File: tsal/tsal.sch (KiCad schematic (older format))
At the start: 9 parts, among them Q1 TIP120, Q2 TIP120

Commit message: TSAL Done in a sane manner - schematic, footprint associations and BOM good. No PCB yet
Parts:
- removed D1: 26V, symbol D_Zener
- removed D2: TSAL, symbol LED
- removed Q1, Q2: TIP120, TO-220, symbol TIP120
- removed R1, R4: 1R, symbol R
- removed R2: 100R, symbol R
- removed R3: 15k, symbol R
- added C1, C3: 10u, Capacitors_ThroughHole:CP_Radial_D5.0mm_P2.00mm, symbol C
- added C2, C4: 1u, Capacitors_ThroughHole:C_Rect_L7.2mm_W5.5mm_P5.00mm_FKS2_FKP2_MKS2_MKP2, symbol C
- added P1: TS+, Wire_Pads:SolderWirePad_single_2mmDrill, symbol CONN_01X01
- added P2: TS-, Wire_Pads:SolderWirePad_single_2mmDrill, symbol CONN_01X01
- added P3: +12V, Wire_Pads:SolderWirePad_2x_2mmDrill, symbol CONN_01X02
- added P4: TS-, Wire_Pads:SolderWirePad_2x_2mmDrill, symbol CONN_01X02
- added U1: V36SE12004NRFA, UNCAMotorsports:V36SE12004NRFA, symbol V36SE12004NRFA
- F1: value 3A -> Fuse; footprint (none) -> Fuse_Holders_and_Fuses:Fuse_SMD1206_HandSoldering
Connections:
- net labels added: GND
- net labels removed: TractiveSystem+, TractiveSystem-
- wire segments 12 -> 18
- no-connect marks 0 -> 1

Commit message: TSAL Updates
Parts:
- added P5: TS+ (PostAIR), Wire_Pads:SolderWirePad_single_1mmDrill, symbol CONN_01X01
- added R1: 10k, Resistors_SMD:R_0805_HandSoldering, symbol R
- added R2: 1k, Resistors_SMD:R_0805_HandSoldering, symbol R
- added U2: TL431, symbol TL431
- P1: value TS+ -> TS+ (PreAIR)
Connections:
- net GND: now also R2.2, U2.3 (A); no longer U1.2 (ON/OFF)
- new net: U1.2 (ON/OFF), U2.1 (C)
- new net: R1.2, R2.1, U2.2 (REF)
- new net: P5.1 (P1), R1.1
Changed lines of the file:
@@
 	1    0    0    -1
 $EndComp
-Wire Wire Line
-	3400 3400 3400 3850
-Wire Wire Line
-	1600 3700 3400 3700
-Wire Wire Line
-	2250 3100 3400 3100
-Connection ~ 3400 3400
-Connection ~ 3400 3700
 NoConn ~ 4600 3400
-Wire Wire Line
-	4600 3250 4600 3100
-Wire Wire Line
-	4600 3550 4600 3850
-Connection ~ 4600 3250
-Connection ~ 4600 3100
-Connection ~ 4600 3550
-Connection ~ 4600 3700
-Connection ~ 3400 3100
-Wire Wire Line
-	4600 3100 6350 3100
-Wire Wire Line
-	4600 3700 6350 3700
 $Comp
 L C C2
@@
 	1    0    0    -1
 $EndComp
-Wire Wire Line
-	5150 3100 5150 3250
-Wire Wire Line
-	5500 3100 5500 3250
-Connection ~ 5150 3100
-Wire Wire Line
-	5150 3700 5150 3550
-Wire Wire Line
-	5500 3700 5500 3550
-Connection ~ 5150 3700
-Wire Wire Line
-	2850 3100 2850 3250
-Wire Wire Line
-	2850 3700 2850 3550
-Wire Wire Line
-	2500 3100 2500 3250
-Connection ~ 2850 3100
-Wire Wire Line
-	2500 3550 2500 3700
-Connection ~ 2850 3700
 $Comp
 L Fuse F1
@@
 	0    1    1    0
 $EndComp
-Connection ~ 2500 3100
-Connection ~ 2500 3700
 $Comp
 L GND #PWR01
@@
 	1    0    0    -1
 $EndComp
-Wire Wire Line
-	6350 3200 5500 3200
-Connection ~ 5500 3200
-Connection ~ 5500 3100
-Wire Wire Line
-	6350 3600 5500 3600
-Connection ~ 5500 3600
-Connection ~ 5500 3700
 $Comp
 L CONN_01X01 P1
@@
 P 1400 3100
 F 0 "P1" H 1319 2875 50  0000 C CNN
-F 1 "TS+" H 1319 2966 50  0000 C CNN
+F 1 "TS+ (PreAIR)" H 1319 2966 50  0000 C CNN
 F 2 "Wire_Pads:SolderWirePad_single_2mmDrill" H 1400 3100 50  0001 C CNN
 F 3 "" H 1400 3100 50  0000 C CNN
@@
 	-1   0    0    1
 $EndComp
-Wire Wire Line
-	1600 3100 1950 3100
 $Comp
 L PWR_FLAG #FLG03
@@
 	1    0    0    -1
 $EndComp
-Connection ~ 1750 3100
+$Comp
+L TL431 U2
+U 1 1 58AFA4D2
+P 2550 4500
+F 0 "U2" H 2371 4553 60  0000 R CNN
+F 1 "TL431" H 2371 4447 60  0000 R CNN
+F 2 "" H 2550 4450 60  0001 C CNN
+F 3 "" H 2550 4450 60  0000 C CNN
+	1    2550 4500
+	-1   0    0    -1
+$EndComp
+$Comp
+L R R1
+U 1 1 58AFA803
+P 2050 4250
+F 0 "R1" H 2120 4296 50  0000 L CNN
+F 1 "10k" H 2120 4205 50  0000 L CNN
+F 2 "Resistors_SMD:R_0805_HandSoldering" V 1980 4250 50  0001 C CNN
+F 3 "" H 2050 4250 50  0000 C CNN
+	1    2050 4250
+	1    0    0    -1
+$EndComp
+$Comp
+L R R2
+U 1 1 58AFA870
+P 2050 4750
+F 0 "R2" H 2120 4796 50  0000 L CNN
+F 1 "1k" H 2120 4705 50  0000 L CNN
+F 2 "Resistors_SMD:R_0805_HandSoldering" V 1980 4750 50  0001 C CNN
+F 3 "" H 2050 4750 50  0000 C CNN
+	1    2050 4750
+	1    0    0    -1
+$EndComp
+$Comp
+L GND #PWR04
+U 1 1 58AFA9A0
+P 2050 5150
+F 0 "#PWR04" H 2050 4900 50  0001 C CNN
+F 1 "GND" H 2055 4977 50  0000 C CNN
+F 2 "" H 2050 5150 50  0000 C CNN
+F 3 "" H 2050 5150 50  0000 C CNN
+	1    2050 5150
+	1    0    0    -1
+$EndComp
+$Comp
+L GND #PWR05
+U 1 1 58AFA9D5
+P 2550 5150
+F 0 "#PWR05" H 2550 4900 50  0001 C CNN
+F 1 "GND" H 2555 4977 50  0000 C CNN
+F 2 "" H 2550 5150 50  0000 C CNN
+F 3 "" H 2550 5150 50  0000 C CNN
+	1    2550 5150
+	1    0    0    -1
+$EndComp
+Wire Wire Line
+	1600 3700 3400 3700
+Wire Wire Line
+	2250 3100 3400 3100
+Connection ~ 3400 3700
+Wire Wire Line
+	4600 3250 4600 3100
+Wire Wire Line
+	4600 3550 4600 3850
+Connection ~ 4600 3250
+Connection ~ 4600 3100
+Connection ~ 4600 3550
+Connection ~ 4600 3700
+Connection ~ 3400 3100
+Wire Wire Line
+	4600 3100 6350 3100
+Wire Wire Line
+	4600 3700 6350 3700
+Wire Wire Line
+	5150 3100 5150 3250
+Wire Wire Line
+	5500 3100 5500 3250
+Connection ~ 5150 3100
+Wire Wire Line
+	5150 3700 5150 3550
+Wire Wire Line
+	5500 3700 5500 3550
+Connection ~ 5150 3700
+Wire Wire Line
+	2850 3100 2850 3250
+Wire Wire Line
+	2850 3700 2850 3550
+Wire Wire Line
+	2500 3100 2500 3250
+Connection ~ 2850 3100
+Wire Wire Line
+	2500 3550 2500 3700
+Connection ~ 2850 3700
+Connection ~ 2500 3100
+Connection ~ 2500 3700
+Wire Wire Line
+	6350 3200 5500 3200
+Connection ~ 5500 3200
+Connection ~ 5500 3100
+Wire Wire Line
+	6350 3600 5500 3600
+Connection ~ 5500 3600
+Connection ~ 5500 3700
+Wire Wire Line
+	1600 3100 1950 3100
+Connection ~ 2050 4500
+Wire Wire Line
+	2050 4500 2200 4500
+Wire Wire Line
+	2550 4100 2550 4200
+Wire Wire Line
+	3400 3400 3250 3400
+Wire Wire Line
+	3250 3400 3250 4100
+Wire Wire Line
+	3250 4100 2550 4100
+Wire Wire Line
+	2550 4800 2550 5150
+Wire Wire Line
+	2050 5150 2050 4900
+Wire Wire Line
+	3400 3700 3400 3850
+$Comp
+L CONN_01X01 P5
+U 1 1 58AFBE9A
+P 1400 4100
+F 0 "P5" H 1319 3875 50  0000 C CNN
+F 1 "TS+ (PostAIR)" H 1319 3966 50  0000 C CNN
+F 2 "Wire_Pads:SolderWirePad_single_1mmDrill" H 1400 4100 50  0001 C CNN
+F 3 "" H 1400 4100 50  0000 C CNN
+	1    1400 4100
+	-1   0    0    1
+$EndComp
+Wire Wire Line
+	2050 4400 2050 4600
+Wire Wire Line
+	2050 4100 1600 4100
 $EndSCHEMATC

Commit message: Not sure what i changed
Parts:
- removed P3: +12V, Wire_Pads:SolderWirePad_2x_2mmDrill, symbol CONN_01X02
- removed P4: TS-, Wire_Pads:SolderWirePad_2x_2mmDrill, symbol CONN_01X02
- added P3, P4, P6, P7: CONN_01X01, Wire_Pads:SolderWirePad_single_2mmDrill, symbol CONN_01X01
- U2: footprint (none) -> TO_SOT_Packages_SMD:SOT-23_Handsoldering
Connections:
- net GND: now also P6.1 (P1), P7.1 (P1)
- net at C3.1, C4.1, U1.7 (+Sense)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: now also P3.1 (P1), P4.1 (P1)
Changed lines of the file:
@@
-$EndComp
-$Comp
-L CONN_01X02 P3
-U 1 1 58AE5670
-P 6550 3150
-F 0 "P3" H 6627 3191 50  0000 L CNN
-F 1 "+12V" H 6627 3100 50  0000 L CNN
-F 2 "Wire_Pads:SolderWirePad_2x_2mmDrill" H 6550 3150 50  0001 C CNN
-F 3 "" H 6550 3150 50  0000 C CNN
-	1    6550 3150
-	1    0    0    -1
-$EndComp
-$Comp
-L CONN_01X02 P4
-U 1 1 58AE5698
-P 6550 3650
-F 0 "P4" H 6627 3691 50  0000 L CNN
-F 1 "TS-" H 6627 3600 50  0000 L CNN
-F 2 "Wire_Pads:SolderWirePad_2x_2mmDrill" H 6550 3650 50  0001 C CNN
-F 3 "" H 6550 3650 50  0000 C CNN
-	1    6550 3650
-	1    0    0    -1
 $EndComp
 $Comp
@@
 F 0 "U2" H 2371 4553 60  0000 R CNN
 F 1 "TL431" H 2371 4447 60  0000 R CNN
-F 2 "" H 2550 4450 60  0001 C CNN
+F 2 "TO_SOT_Packages_SMD:SOT-23_Handsoldering" H 2550 4450 60  0001 C CNN
 F 3 "" H 2550 4450 60  0000 C CNN
 	1    2550 4500
@@
 Wire Wire Line
 	2050 4100 1600 4100
+$Comp
+L CONN_01X01 P3
+U 1 1 58AFAF9A
+P 6550 3100
+F 0 "P3" H 6628 3141 50  0000 L CNN
+F 1 "CONN_01X01" H 6628 3050 50  0000 L CNN
+F 2 "Wire_Pads:SolderWirePad_single_2mmDrill" H 6550 3100 50  0001 C CNN
+F 3 "" H 6550 3100 50  0000 C CNN
+	1    6550 3100
+	1    0    0    -1
+$EndComp
+$Comp
+L CONN_01X01 P4
+U 1 1 58AFAFD8
+P 6550 3300
+F 0 "P4" H 6628 3341 50  0000 L CNN
+F 1 "CONN_01X01" H 6628 3250 50  0000 L CNN
+F 2 "Wire_Pads:SolderWirePad_single_2mmDrill" H 6550 3300 50  0001 C CNN
+F 3 "" H 6550 3300 50  0000 C CNN
+	1    6550 3300
+	1    0    0    -1
+$EndComp
+$Comp
+L CONN_01X01 P7
+U 1 1 58AFB014
+P 6550 3700
+F 0 "P7" H 6628 3741 50  0000 L CNN
+F 1 "CONN_01X01" H 6628 3650 50  0000 L CNN
+F 2 "Wire_Pads:SolderWirePad_single_2mmDrill" H 6550 3700 50  0001 C CNN
+F 3 "" H 6550 3700 50  0000 C CNN
+	1    6550 3700
+	1    0    0    -1
+$EndComp
+$Comp
+L CONN_01X01 P6
+U 1 1 58AFB052
+P 6550 3500
+F 0 "P6" H 6628 3541 50  0000 L CNN
+F 1 "CONN_01X01" H 6628 3450 50  0000 L CNN
+F 2 "Wire_Pads:SolderWirePad_single_2mmDrill" H 6550 3500 50  0001 C CNN
+F 3 "" H 6550 3500 50  0000 C CNN
+	1    6550 3500
+	1    0    0    -1
+$EndComp
+Wire Wire Line
+	6350 3300 6350 3200
+Wire Wire Line
+	6350 3500 6350 3600
 $EndSCHEMATC

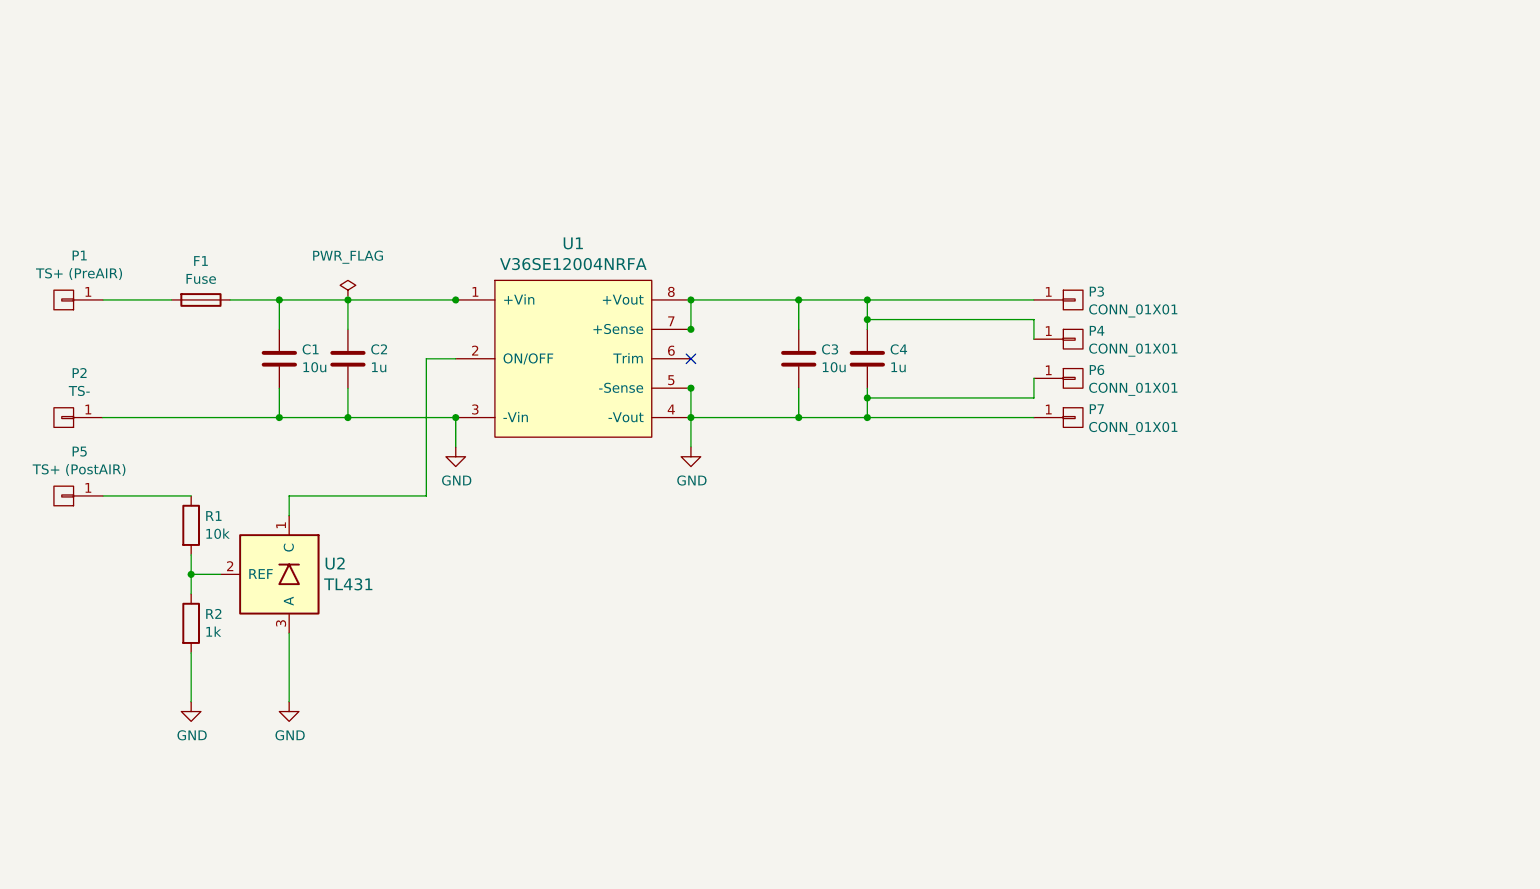
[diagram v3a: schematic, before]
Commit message: Update TSAL to comply with ESF Feedback
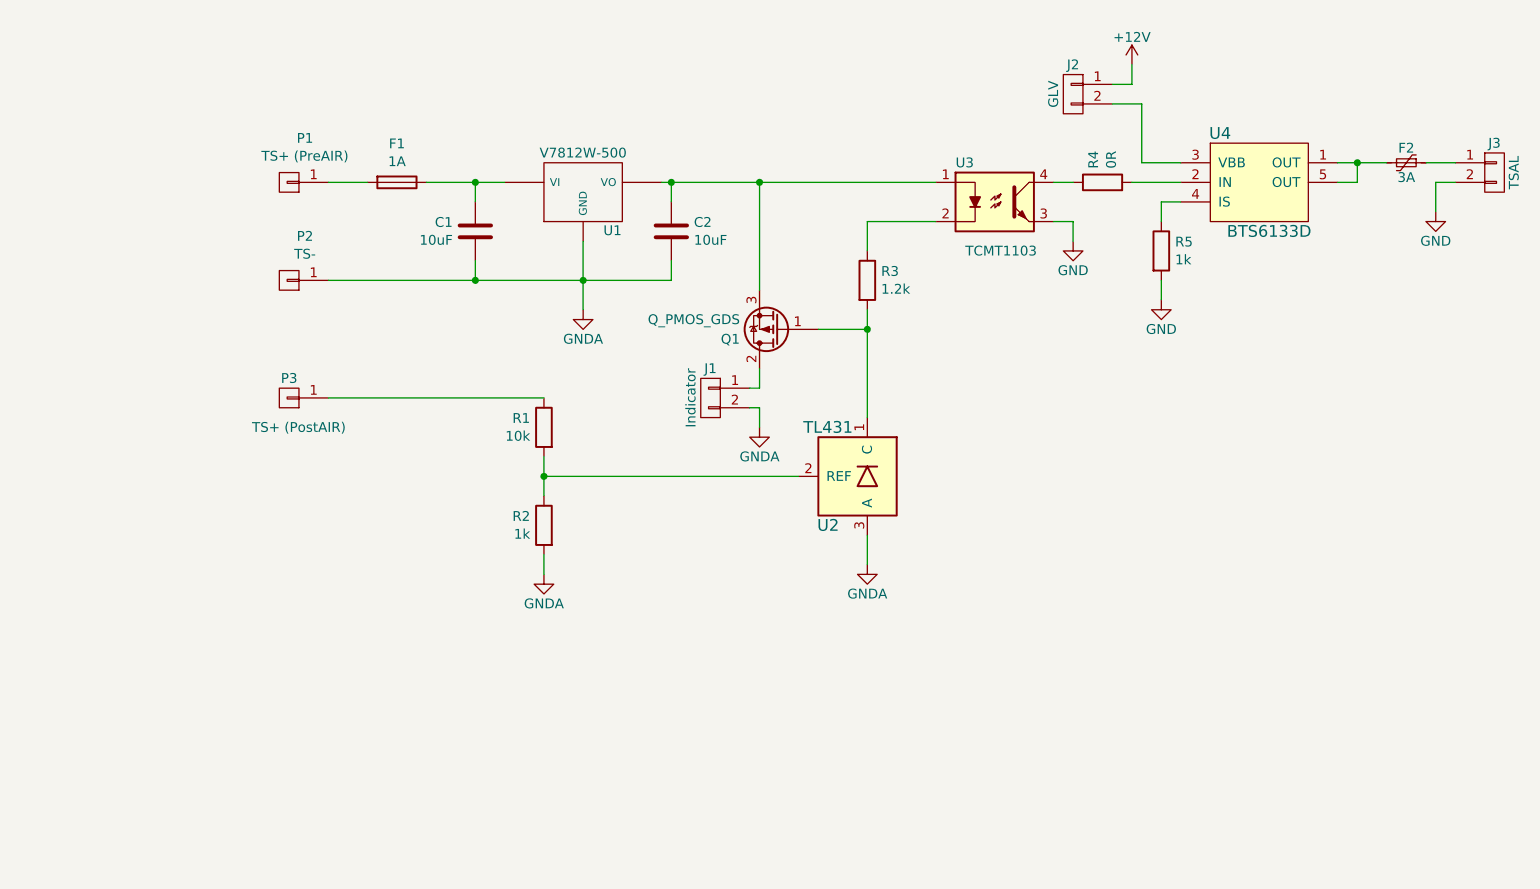
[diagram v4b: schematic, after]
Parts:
- removed C3: 10u, Capacitors_ThroughHole:CP_Radial_D5.0mm_P2.00mm, symbol C
- removed C4: 1u, Capacitors_ThroughHole:C_Rect_L7.2mm_W5.5mm_P5.00mm_FKS2_FKP2_MKS2_MKP2, symbol C
- removed P4, P6, P7: CONN_01X01, Wire_Pads:SolderWirePad_single_2mmDrill, symbol CONN_01X01
- removed P5: TS+ (PostAIR), Wire_Pads:SolderWirePad_single_1mmDrill, symbol CONN_01X01
- removed U1: V36SE12004NRFA, UNCAMotorsports:V36SE12004NRFA, symbol V36SE12004NRFA
- added F2: 3A, symbol Polyfuse_Small
- added J1: Indicator, symbol CONN_01X02
- added J2: GLV, symbol CONN_01X02
- added J3: TSAL, symbol CONN_01X02
- added Q1: Q_PMOS_GDS, symbol Q_PMOS_GDS
- added R3: 1.2k, Resistors_SMD:R_0805_HandSoldering, symbol R
- added R4: 0R, Resistors_SMD:R_0805_HandSoldering, symbol R
- added R5: 1k, Resistors_SMD:R_0805_HandSoldering, symbol R
- added U1: V7812W-500, symbol V7812W-500
- added U3: TCMT1103, UNCAMotorsports:SSOP-4, symbol TCMT1103
- added U4: BTS6133D, symbol BTS6133D
- C1: value 10u -> 10uF
- C2: value 1u -> 10uF; footprint Capacitors_ThroughHole:C_Rect_L7.2mm_W5.5mm_P5.00mm_FKS2_FKP2_MKS2_MKP2 -> Capacitors_ThroughHole:CP_Radial_D5.0mm_P2.00mm
- F1: value Fuse -> 1A
- P3: value CONN_01X01 -> TS+ (PostAIR); footprint Wire_Pads:SolderWirePad_single_2mmDrill -> Wire_Pads:SolderWirePad_single_1mmDrill
- U2: footprint TO_SOT_Packages_SMD:SOT-23_Handsoldering -> (none)
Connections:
- net GND: now also J3.2 (P2), R5.2, U3.3; no longer C1.2, C2.2, P2.1 (P1), R2.2, U2.3 (A)
- net at C1.1, F1.1: now also U1.1 (VI); no longer C2.1
- net at U2.1 (C): now also Q1.1 (G), R3.2
- net at P3.1 (P1): now also R1.1
- new net: F2.1, J3.1 (P1)
- new net: F2.2, U4.1 (OUT), U4.5 (OUT)
- new net: R4.2, U4.2 (IN)
- new net: J2.2 (P2), U4.3 (VBB)
- new net: R5.1, U4.4 (IS)
- new net: R4.1, U3.4
- new net: C2.1, Q1.3 (S), U1.3 (VO), U3.1
- new net: R3.1, U3.2
- new net: J1.1 (P1), Q1.2 (D)
- new net +12V: J2.1 (P1)
- new net GNDA: C1.2, C2.2, J1.2 (P2), P2.1 (P1), R2.2, U1.2 (GND), U2.3 (A)
- no-connect marks 1 -> 0
